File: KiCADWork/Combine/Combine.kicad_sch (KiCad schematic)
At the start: 0 parts

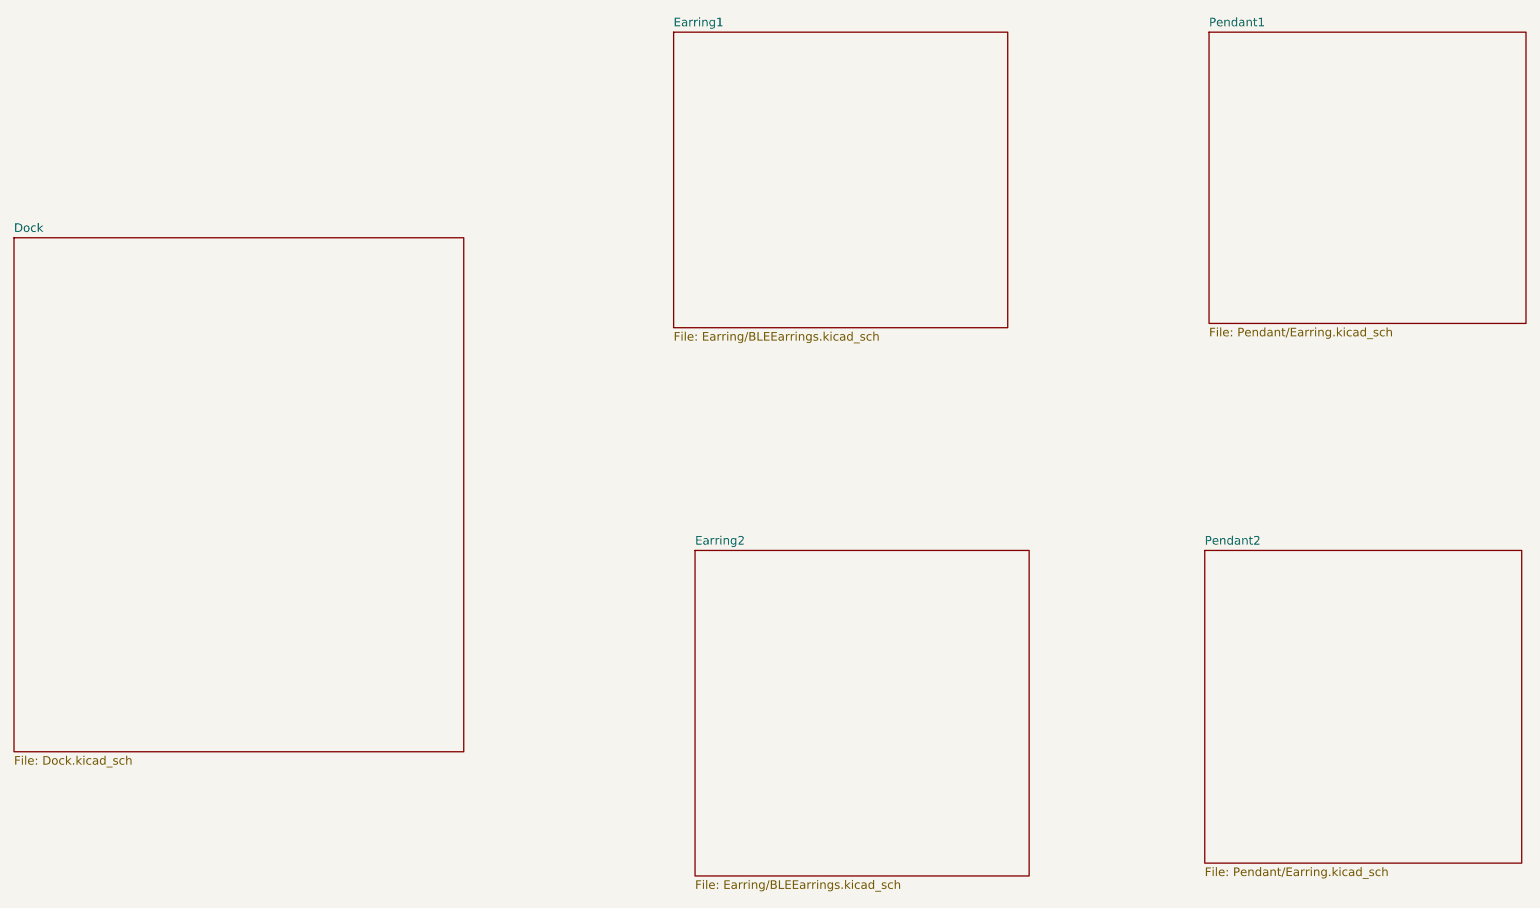
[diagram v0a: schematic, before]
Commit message: Completing the combined layout
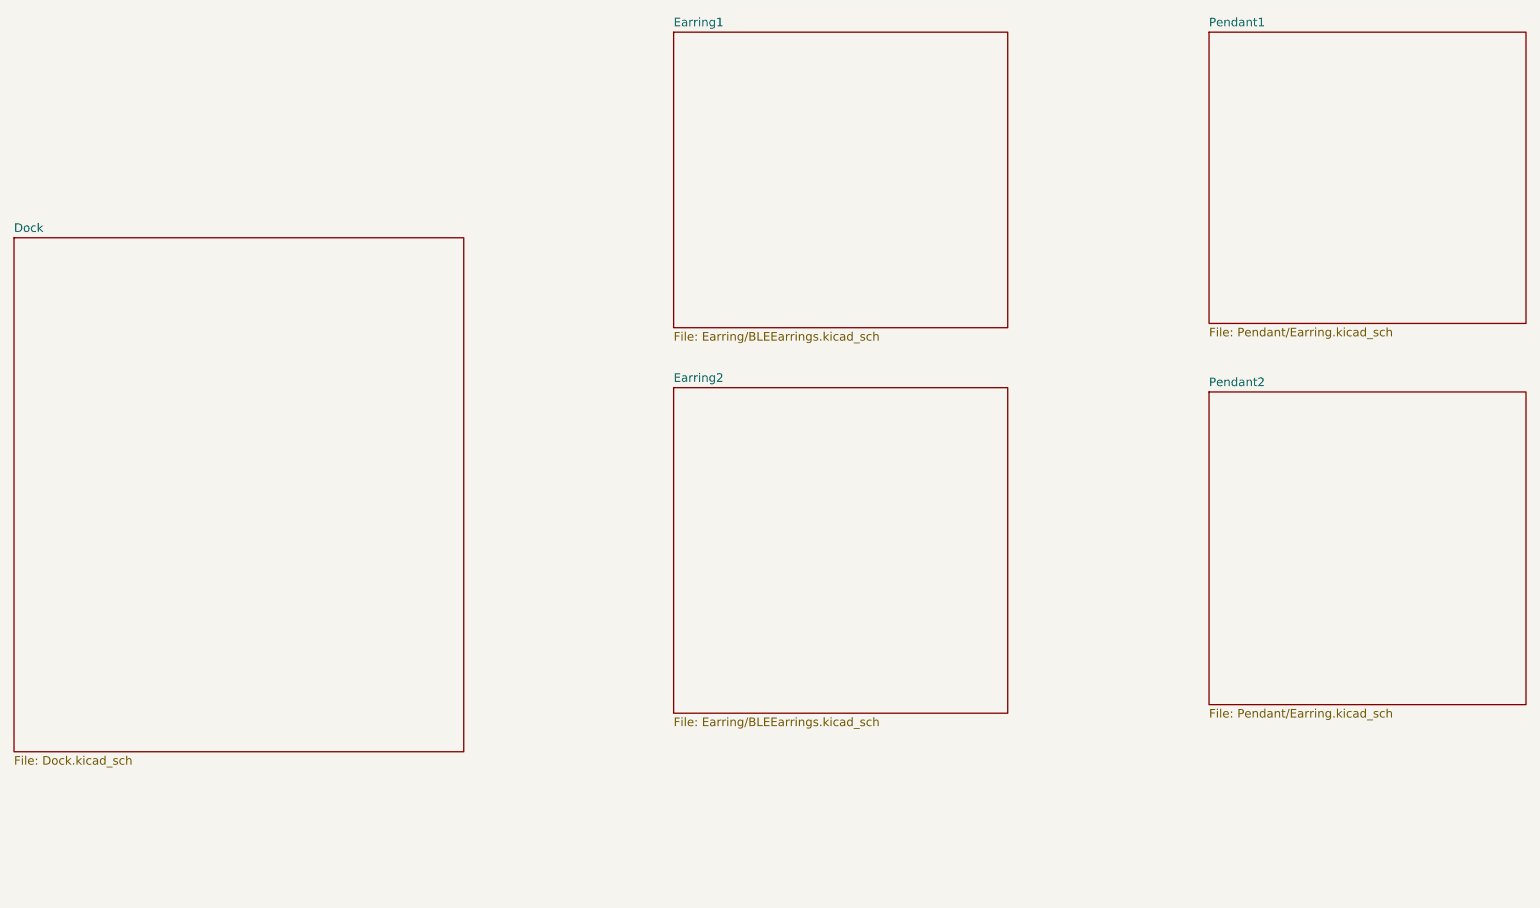
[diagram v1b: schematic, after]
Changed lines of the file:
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@@
     )
   )
-  (sheet (at 207.01 103.505) (size 46.99 46.355) (fields_autoplaced)
+  (sheet (at 207.645 80.01) (size 46.99 46.355) (fields_autoplaced)
     (stroke (width 0.1524) (type solid))
     (fill (color 0 0 0 0.0000))
-    (property "Sheetname" "Pendant2" (at 207.01 102.7934 0)
+    (property "Sheetname" "Pendant2" (at 207.645 79.2984 0)
       (effects (font (size 1.27 1.27)) (justify left bottom))
     )
-    (property "Sheetfile" "Pendant/Earring.kicad_sch" (at 207.01 150.4446 0)
+    (property "Sheetfile" "Pendant/Earring.kicad_sch" (at 207.645 126.9496 0)
       (effects (font (size 1.27 1.27)) (justify left top))
     )
@@
     )
   )
-  (sheet (at 131.445 103.505) (size 49.53 48.26) (fields_autoplaced)
+  (sheet (at 128.27 79.375) (size 49.53 48.26) (fields_autoplaced)
     (stroke (width 0.1524) (type solid))
     (fill (color 0 0 0 0.0000))
-    (property "Sheetname" "Earring2" (at 131.445 102.7934 0)
+    (property "Sheetname" "Earring2" (at 128.27 78.6634 0)
       (effects (font (size 1.27 1.27)) (justify left bottom))
     )
-    (property "Sheetfile" "Earring/BLEEarrings.kicad_sch" (at 131.445 152.3496 0)
+    (property "Sheetfile" "Earring/BLEEarrings.kicad_sch" (at 128.27 128.2196 0)
       (effects (font (size 1.27 1.27)) (justify left top))
     )
